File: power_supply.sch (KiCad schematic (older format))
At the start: 65 parts

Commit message: Added comments
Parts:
- added C15, C6: .1uF, symbol C
- added D15: PG, ~, symbol LED
- added R21: 1.5k, ~, symbol R
- gave numbers to parts that had none: 65
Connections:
- wire segments 223 -> 231
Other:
- note added: "Connections and component \nvalues from eval \nboard for MIC2185."
- note added: "Currently 1% Resistors and \n5% Pot (couldn't find them smaller).\nDo you think we could do with lower \naccuracy resistors for this divider network?"
- note added: "Currently assuming that we do not need \nany resistor network on input D+/D-. This\nis easy to change if we find different results\nin our testing."
- note added: "Currently outputing 5V. Should we output slightly above 5V (say 5.1V) \nto account for voltage drops across resistances and wires? I measured\n the output of a few USB chargers that I own and they output slightly \nabove 5V."
- note added: "Decided to stick with two MOSFETs because both the \ndatasheet and eval board suggested this. I also think \nthat it will help somewhat with heat dissipation - as \nabout half of the total power will be going through \neach mosfet. Though that may be a non issue. What \nare your thoughts?"
- note added: "EN/UVLO is used to turn off the device when the \nvoltage is below 1.5V. So we provide a voltage \ndivider which provides this pin with half of the \nsupply voltage. Once the supply voltage reaches \n3.0V (battery is discharged), it turns the boost \nconverter off."
- note added: "FREQ/2 is tied to VDD, which puts the \ndevice into low frequency (200kHz) operation."
- note added: "Gain of 50 and full scale\nvoltage of 1.875. This means\nfull scale voltage drop across\nshunt resistor is 37.5mV."
- note added: "Power Good LED:\nIndicates that the power source is\nsupplying power - i.e. that the\nexternal adapter is plugged in, or\nthat the battery is not fully discharged."
- note added: "This specific chip was chosen because \nit comes in SOT23-5 and because it provides\nESD protection on the VUSB power line as\nwell as the data lines."
- note added: "USB Type A female jack"
- note added: "USB micro type B jack"
- note removed: "Full Scale Voltage: 1.875V"
- moved on the sheet: D11, D12, D14, F1, R11, R22, R6, R7, U6, U7

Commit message: Updating based on Bob's feedback
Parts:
- removed D15: PG, ~, symbol LED
- removed Q2: SI4174DY, ~, symbol SI4174DY
- removed Q3: SI4463CDY, ~, symbol SI4463CDY
- removed R10, R19: 100k, symbol POT
- removed R13, R17: 26.1, ~, symbol R
- removed R14, R18: 100k, ~, symbol R
- removed R21: 1.5k, ~, symbol R
- removed R22: .025, ~, symbol R
- removed U6: TPD2E001DRL, symbol TPD2E001DRL
- added C?: .1uF, symbol C
- added F?: PTC, symbol PTC
- added R?: .05, ~, symbol R-4TERM
- added R?: 34.0k, ~, symbol R
- added U?: TPD2E001DRL, symbol TPD2E001DRL
- added U?: TPS2511, symbol TPS2511
- D13: Digikey Product Number (none) -> B130-E3/5ATGICT-ND
- J1: Digikey Product Number (none) -> A108263CT-ND
- L1: Digikey Product Number (none) -> SRR1240-4R7MCT-ND
- Q1: Digikey Product Number (none) -> SI4174DY-T1-GE3CT-ND
- Q4: Mouser Product Number (none) -> 78-SI4463CDY-T1-GE3
- R11, R6, R7: value 1.5k -> 6k
- R16: value 3.32k -> 31.6k
- U1: Digikey Product Number (none) -> LM3914N-1/NOPB-ND
- U2: Digikey Product Number (none) -> 296-21883-1-ND
- U7: value MAX9938 -> MAX9938T; Digikey Product Number (none) -> MAX9938TEUK+TCT-ND
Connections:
- net labels added: VUSB
- wire segments 231 -> 207
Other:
- note added: "47uF cap is \ntantalum."
- note added: "All three 120uF caps \nare tantalum."
- note added: "LED current set to .5mA - this is bright \nenough for indication purposes."
- note added: "Limits output current to 1.507A"
- note added: "Modified to use resistor \nsuggested in eval board."
- note removed: "Connections and component \nvalues from eval \nboard for MIC2185."
- note removed: "Currently 1% Resistors and \n5% Pot (couldn't find them smaller).\nDo you think we could do with lower \naccuracy resistors for this divider network?"
- note removed: "Currently assuming that we do not need \nany resistor network on input D+/D-. This\nis easy to change if we find different results\nin our testing."
- note removed: "Currently outputing 5V. Should we output slightly above 5V (say 5.1V) \nto account for voltage drops across resistances and wires? I measured\n the output of a few USB chargers that I own and they output slightly \nabove 5V."
- note removed: "Decided to stick with two MOSFETs because both the \ndatasheet and eval board suggested this. I also think \nthat it will help somewhat with heat dissipation - as \nabout half of the total power will be going through \neach mosfet. Though that may be a non issue. What \nare your thoughts?"
- note removed: "EN/UVLO is used to turn off the device when the \nvoltage is below 1.5V. So we provide a voltage \ndivider which provides this pin with half of the \nsupply voltage. Once the supply voltage reaches \n3.0V (battery is discharged), it turns the boost \nconverter off."
- note removed: "FREQ/2 is tied to VDD, which puts the \ndevice into low frequency (200kHz) operation."
- note removed: "Gain of 50 and full scale\nvoltage of 1.875. This means\nfull scale voltage drop across\nshunt resistor is 37.5mV."
- note removed: "Non Inductive Resistor"
- note removed: "Power Good LED:\nIndicates that the power source is\nsupplying power - i.e. that the\nexternal adapter is plugged in, or\nthat the battery is not fully discharged."
- note removed: "This specific chip was chosen because \nit comes in SOT23-5 and because it provides\nESD protection on the VUSB power line as\nwell as the data lines."
- moved on the sheet: C1, C10, C12, C13, C14, C2, C3, C4, C5, C8, C9, D13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

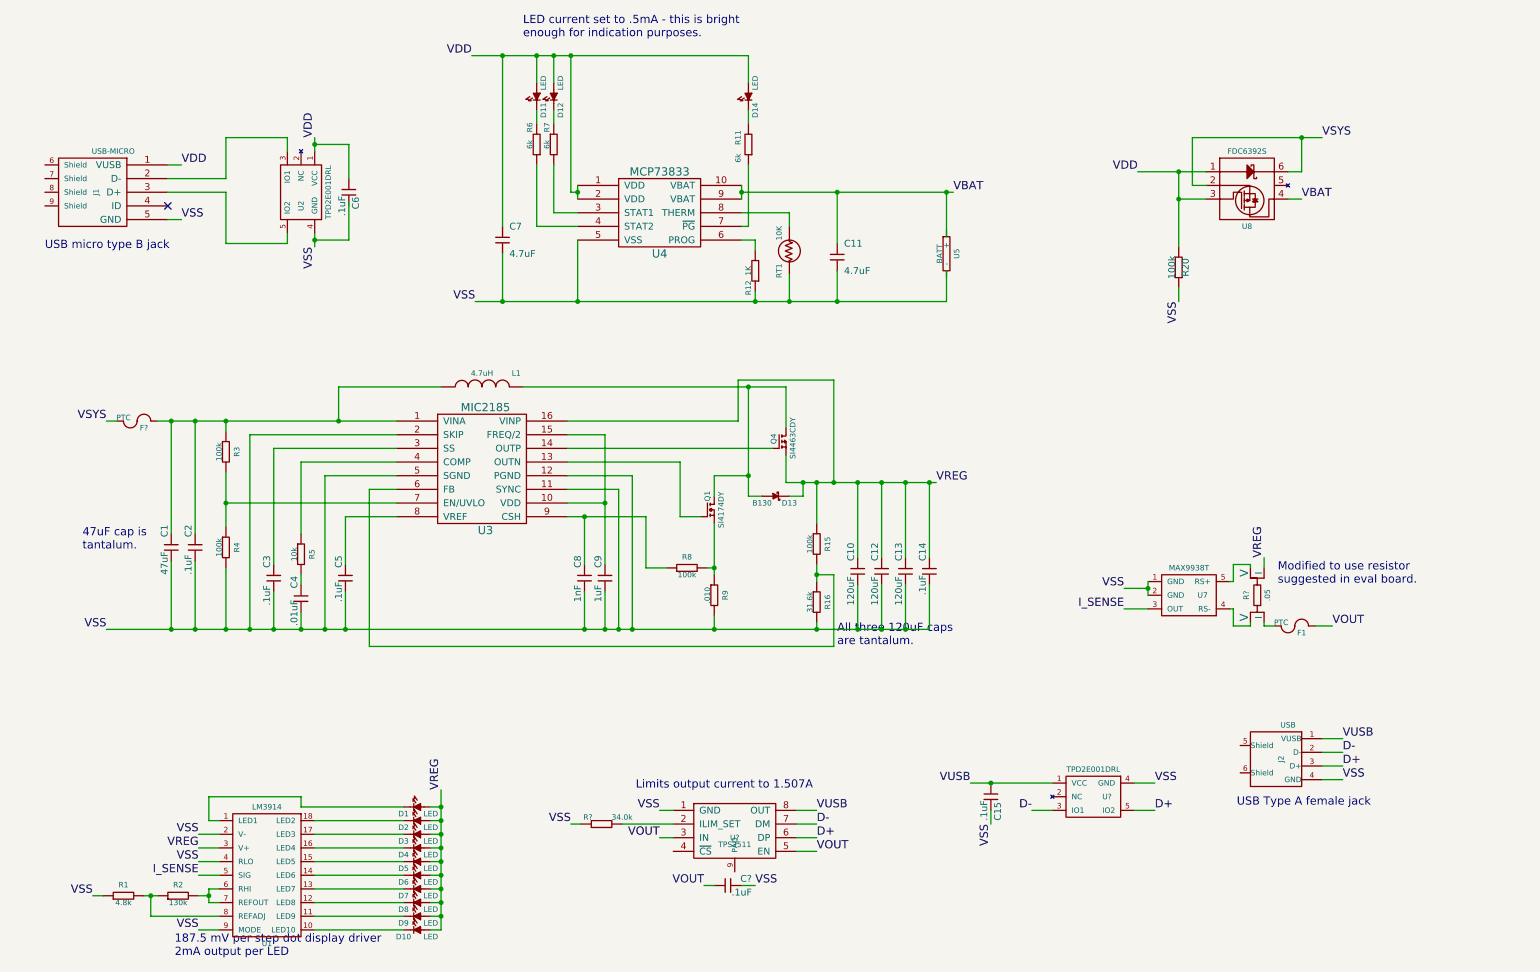
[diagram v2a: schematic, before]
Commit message: Added turn off for display when no current is being drawn
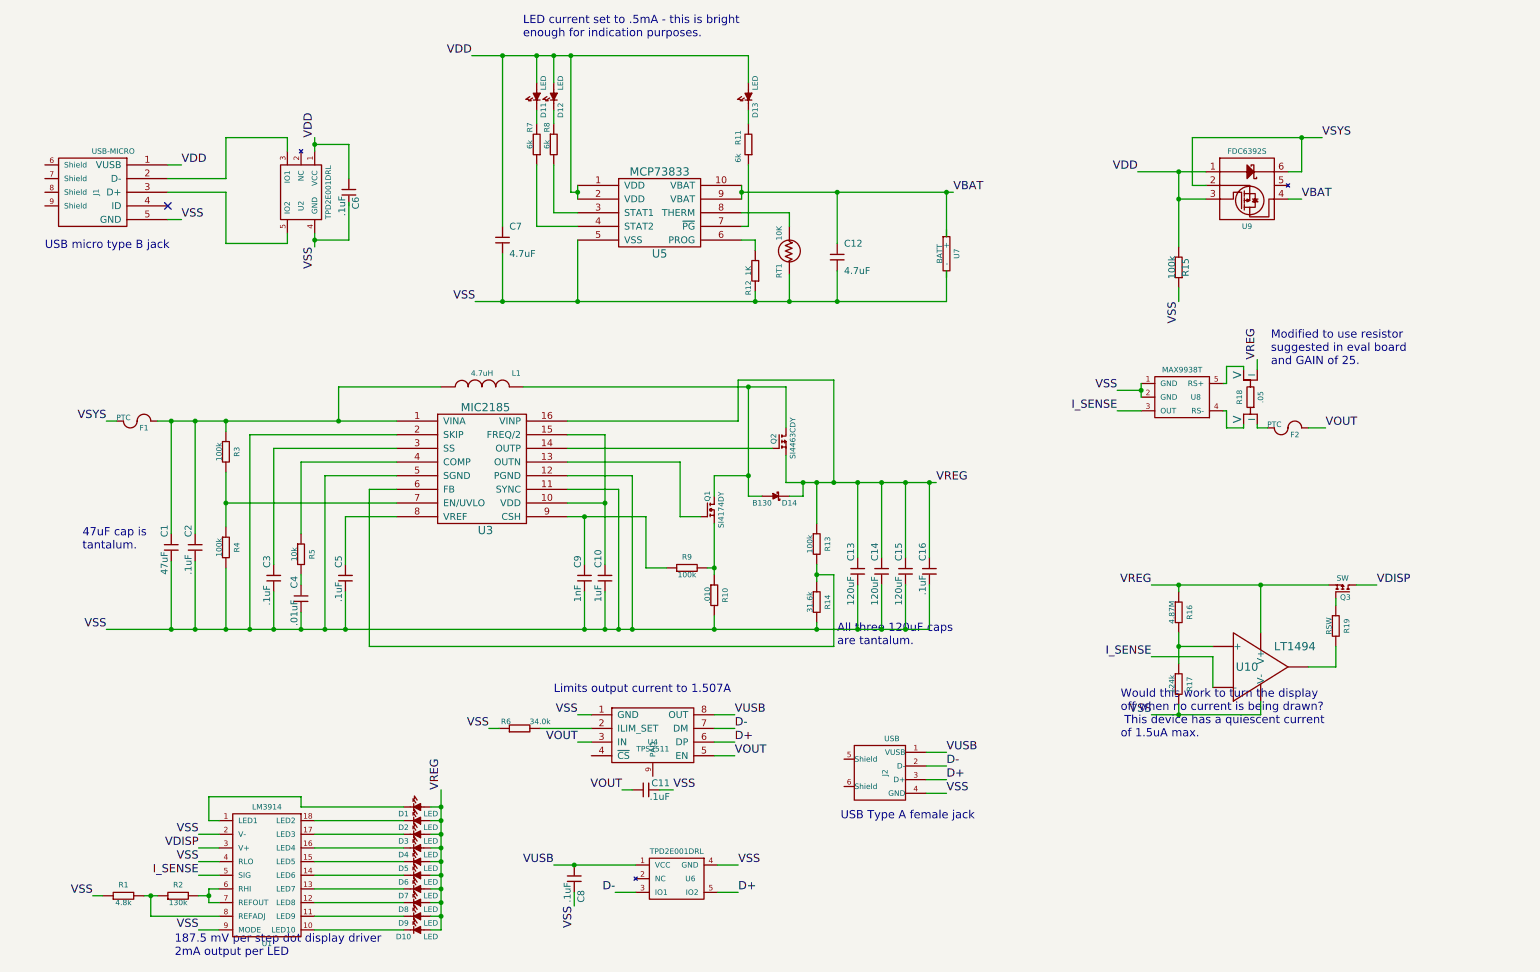
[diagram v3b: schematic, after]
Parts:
- added Q3: SW, ~, symbol SI4463CDY
- added R16: 4.87M, ~, symbol R
- added R17: 124k, ~, symbol R
- added R19: RSW, ~, symbol R
- added U10: LT1494, symbol LT1494
- gave numbers to parts that had none: 6
- renumbered C9 to C10, C11 to C12, C10 to C13, C12 to C14, C13 to C15, C14 to C16, C15 to C8, C8 to C9, D14 to D13, D13 to D14, F1 to F2, Q4 to Q2, R9 to R10, R15 to R13, R16 to R14, R20 to R15, R6 to R7, R7 to R8, R8 to R9, U4 to U5, U5 to U7, U7 to U8, U8 to U9
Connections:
- net I_SENSE: now also U10.2 (-)
- net VREG: now also Q3.S, R16.1, U10.7 (V+); no longer U1.3 (V+)
- net VSS: now also R17.2, U10.4 (V-)
- new net: R16.2, R17.1, U10.3 (+)
- new net: R19.2, U10.6
- new net: Q3.G, R19.1
- new net VDISP: Q3.D, U1.3 (V+)
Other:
- note added: "Modified to use resistor \nsuggested in eval board \nand GAIN of 25."
- note added: "Would this work to turn the display \noff when no current is being drawn?\n This device has a quiescent current \nof 1.5uA max."
- note removed: "Modified to use resistor \nsuggested in eval board."
- moved on the sheet: C11, C8, F2, J2, R18, R6, U4, U6, U8

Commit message: Fixed a few issues with printout
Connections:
- net VSS: no longer R15.1
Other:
- note removed: "Modified to use resistor \nsuggested in eval board \nand GAIN of 25."
- moved on the sheet: C11, C8, D1, D10, D2, D3, D4, D5, D6, D7, D8, D9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

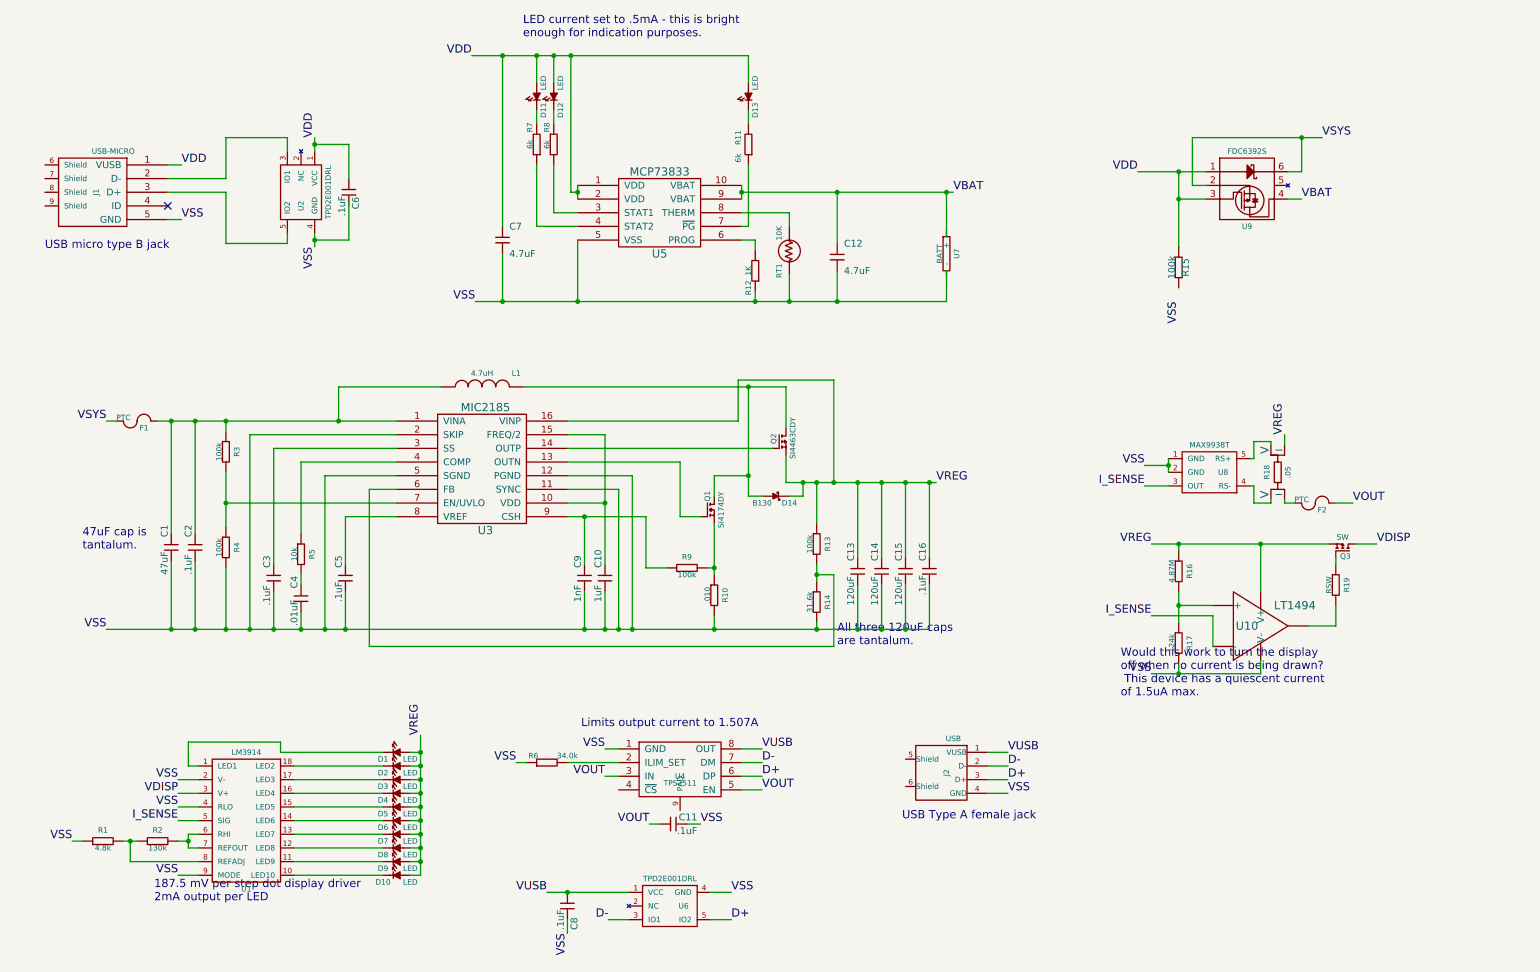
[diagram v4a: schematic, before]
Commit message: Fixed ERC errors
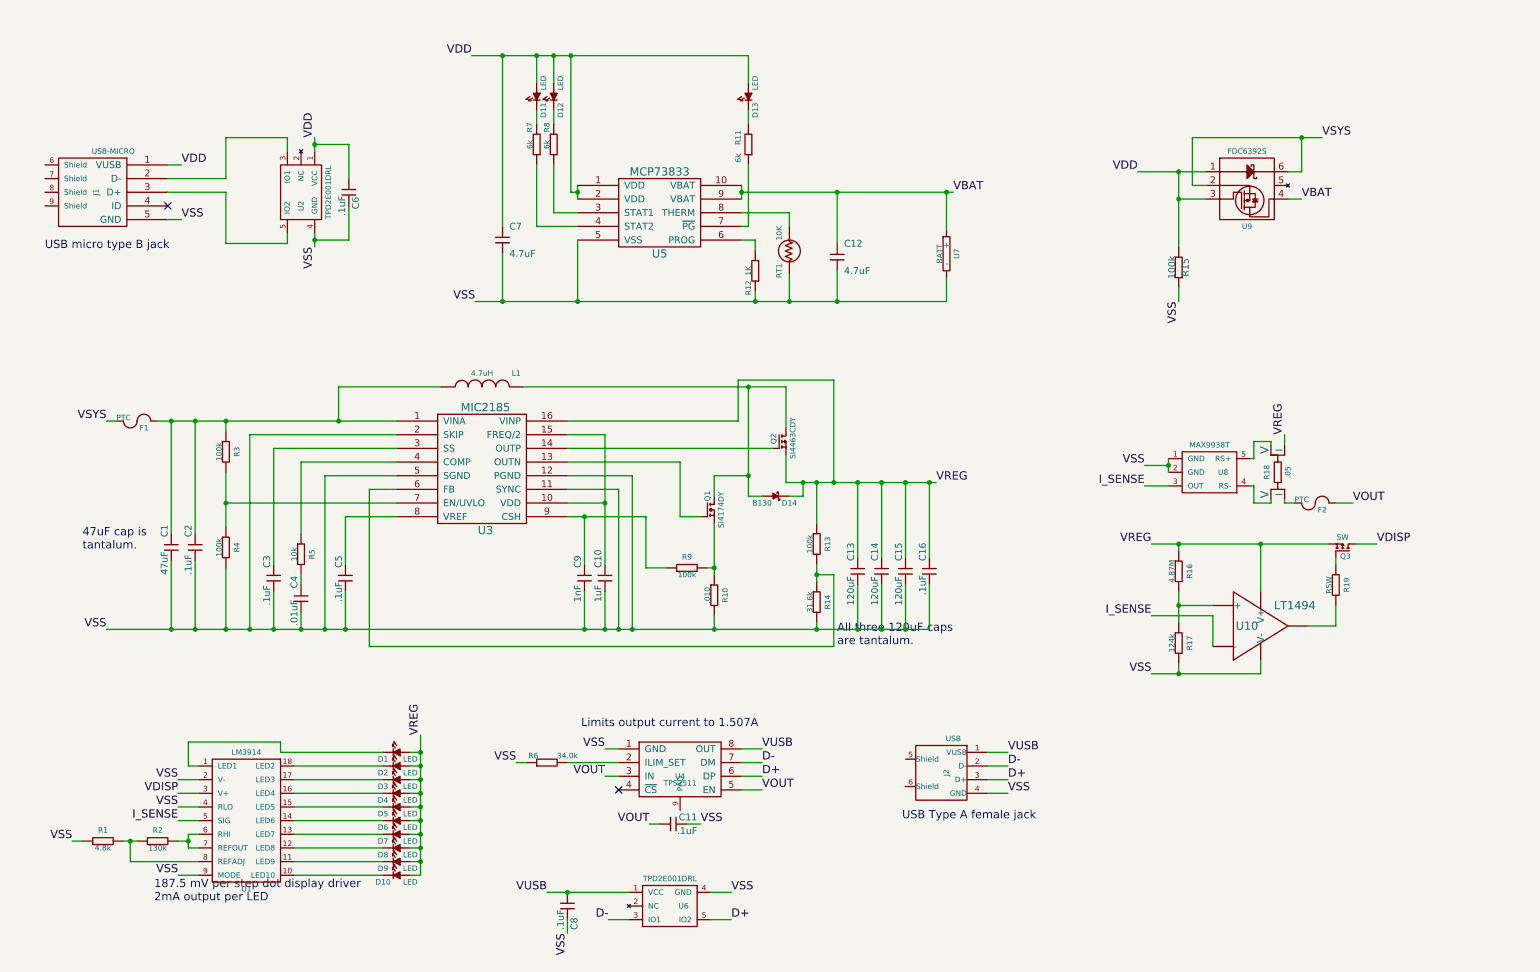
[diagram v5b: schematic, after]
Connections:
- net VBAT: now also U7.1 (+)
- net VSS: now also C6.2, R15.1, U7.2 (-)
- no-connect marks 1 -> 2
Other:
- note removed: "LED current set to .5mA - this is bright \nenough for indication purposes."
- note removed: "Would this work to turn the display \noff when no current is being drawn?\n This device has a quiescent current \nof 1.5uA max."
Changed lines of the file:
@@
 	1    0    0    -1
 $EndComp
-Text Notes 4275 700  0    60   ~ 0
-LED current set to .5mA - this is bright \nenough for indication purposes.
 Text Notes 6575 5150 0    60   ~ 0
 All three 120uF caps \nare tantalum.
@@
 Wire Wire Line
 	6575 2625 6575 2400
-Wire Wire Line
-	7375 2625 7375 2400
 Connection ~ 6575 2625
 Wire Wire Line
@@
 	5875 1825 7425 1825
 Connection ~ 5875 1825
-Wire Wire Line
-	7375 1825 7375 2150
 Connection ~ 7375 1825
 Wire Wire Line
@@
 	3000 1475 2750 1475
 Connection ~ 2750 1475
-Wire Wire Line
-	3000 1900 3000 2175
 Wire Wire Line
 	3000 2175 2750 2175
@@
 Text Label 10525 4400 0    60   ~ 0
 VDISP
-Text Notes 8650 5525 0    60   ~ 0
-Would this work to turn the display \noff when no current is being drawn?\n This device has a quiescent current \nof 1.5uA max.
 Text Label 1750 6225 2    60   ~ 0
 VDISP
@@
 Wire Wire Line
 	9675 4400 9675 4750
+Wire Wire Line
+	9075 2625 9075 2525
+Wire Wire Line
+	3000 1925 3000 2175
+Wire Wire Line
+	7375 2625 7375 2450
+Wire Wire Line
+	7375 2100 7375 1825
+NoConn ~ 4975 6200
 $EndSCHEMATC
